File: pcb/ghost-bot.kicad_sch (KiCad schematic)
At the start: 25 parts, among them J1 Conn_01x03_Pin, J2 Conn_01x03_Pin, J3 Conn_01x02_Pin, J4 Conn_01x04_Pin, SW1 SW_Push

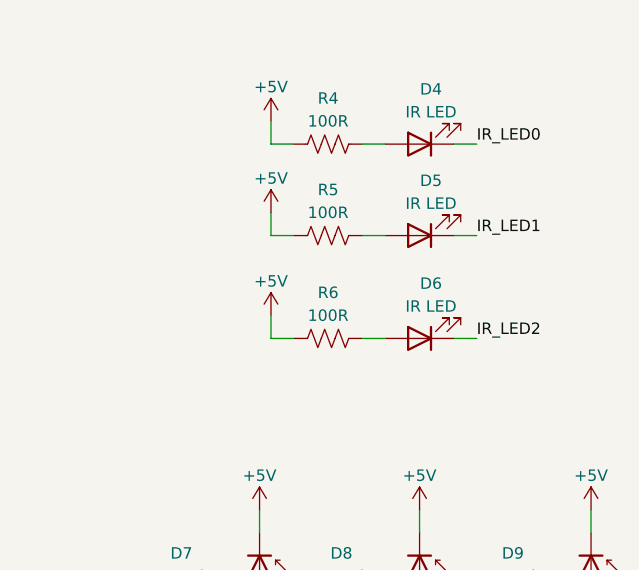
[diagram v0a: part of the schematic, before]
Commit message: Connect IR LEDs to GND
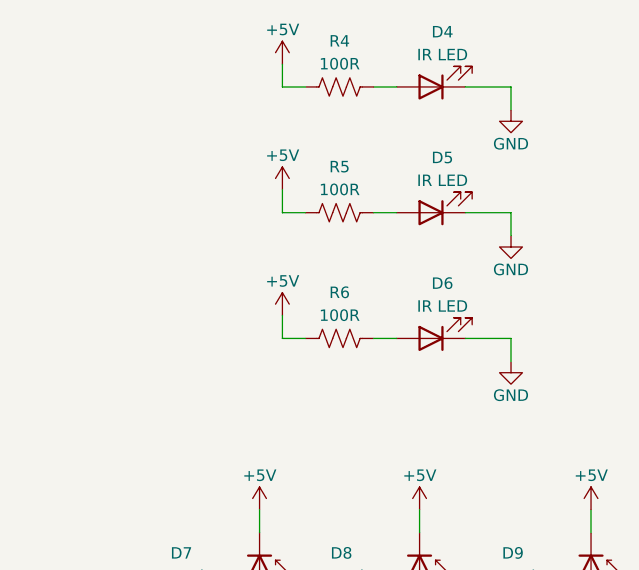
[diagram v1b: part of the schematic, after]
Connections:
- net IR_LED0 is gone; now on net GND: D4.1 (K)
- net IR_LED1 is gone; now on net GND: D5.1 (K)
- net IR_LED2 is gone; now on net GND: D6.1 (K)
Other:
- moved on the sheet: D4, D5, D6, R4, R5, R6

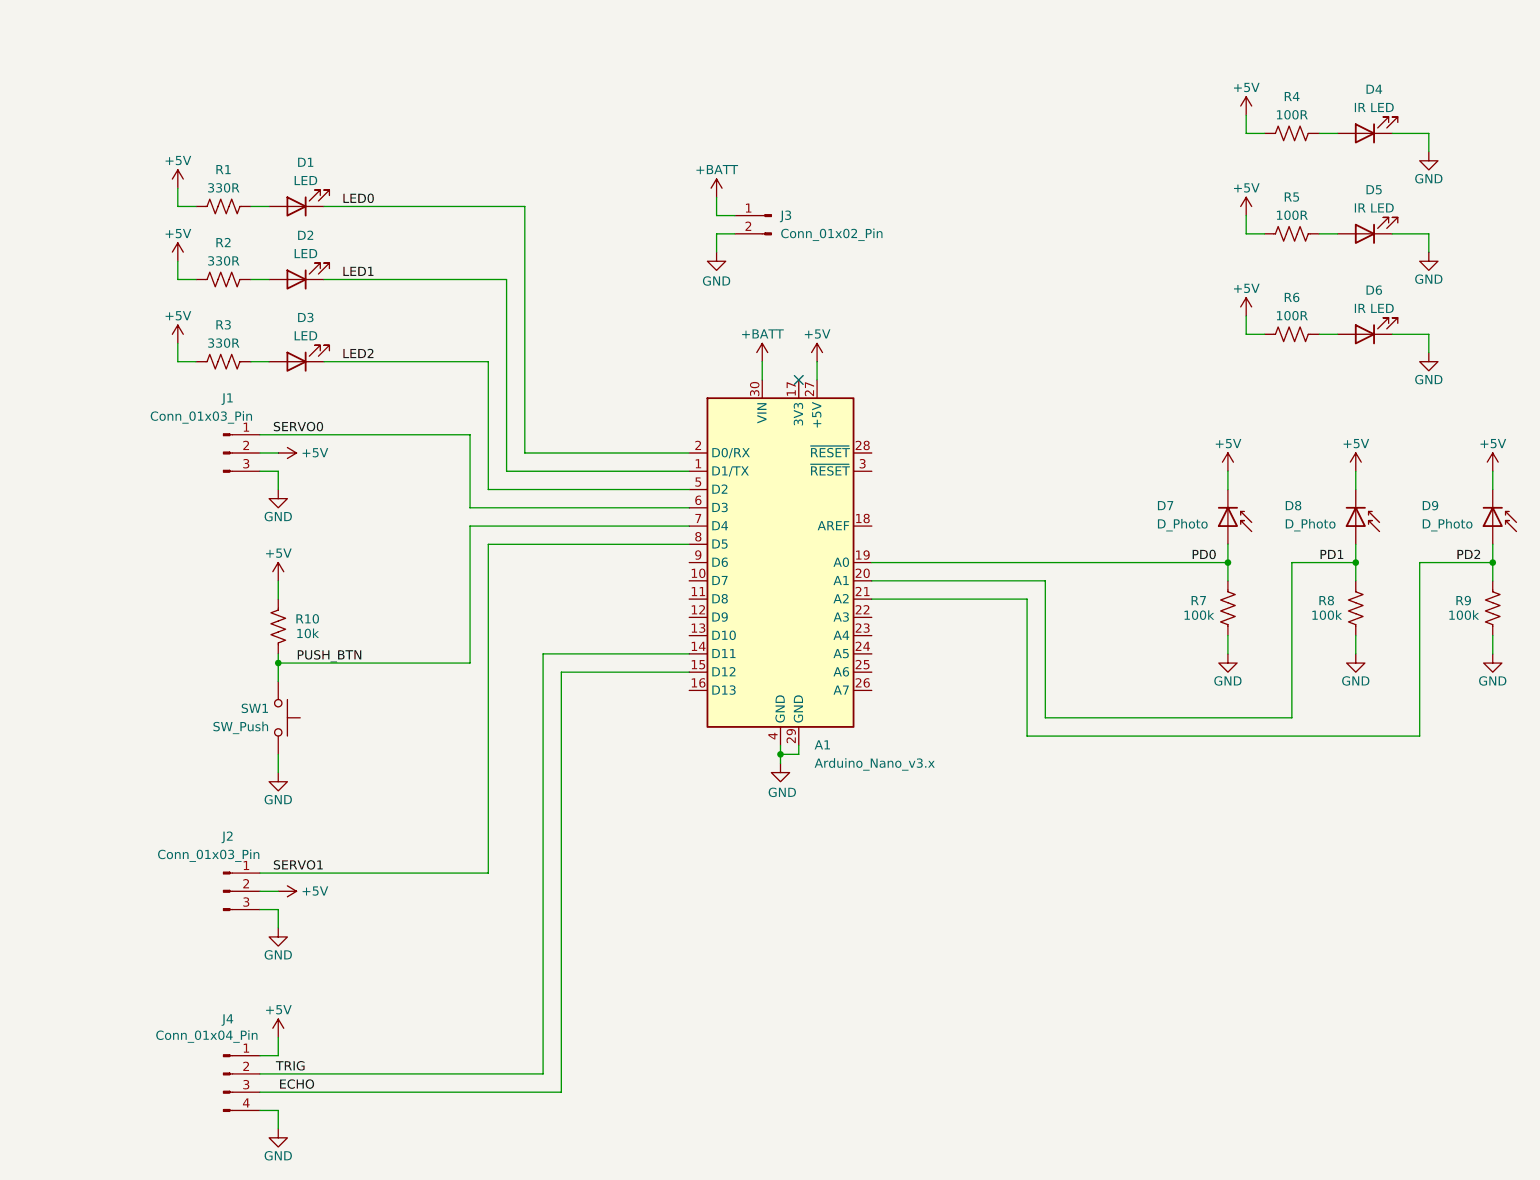
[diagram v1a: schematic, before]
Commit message: Breakout unused pins, add extra power pins
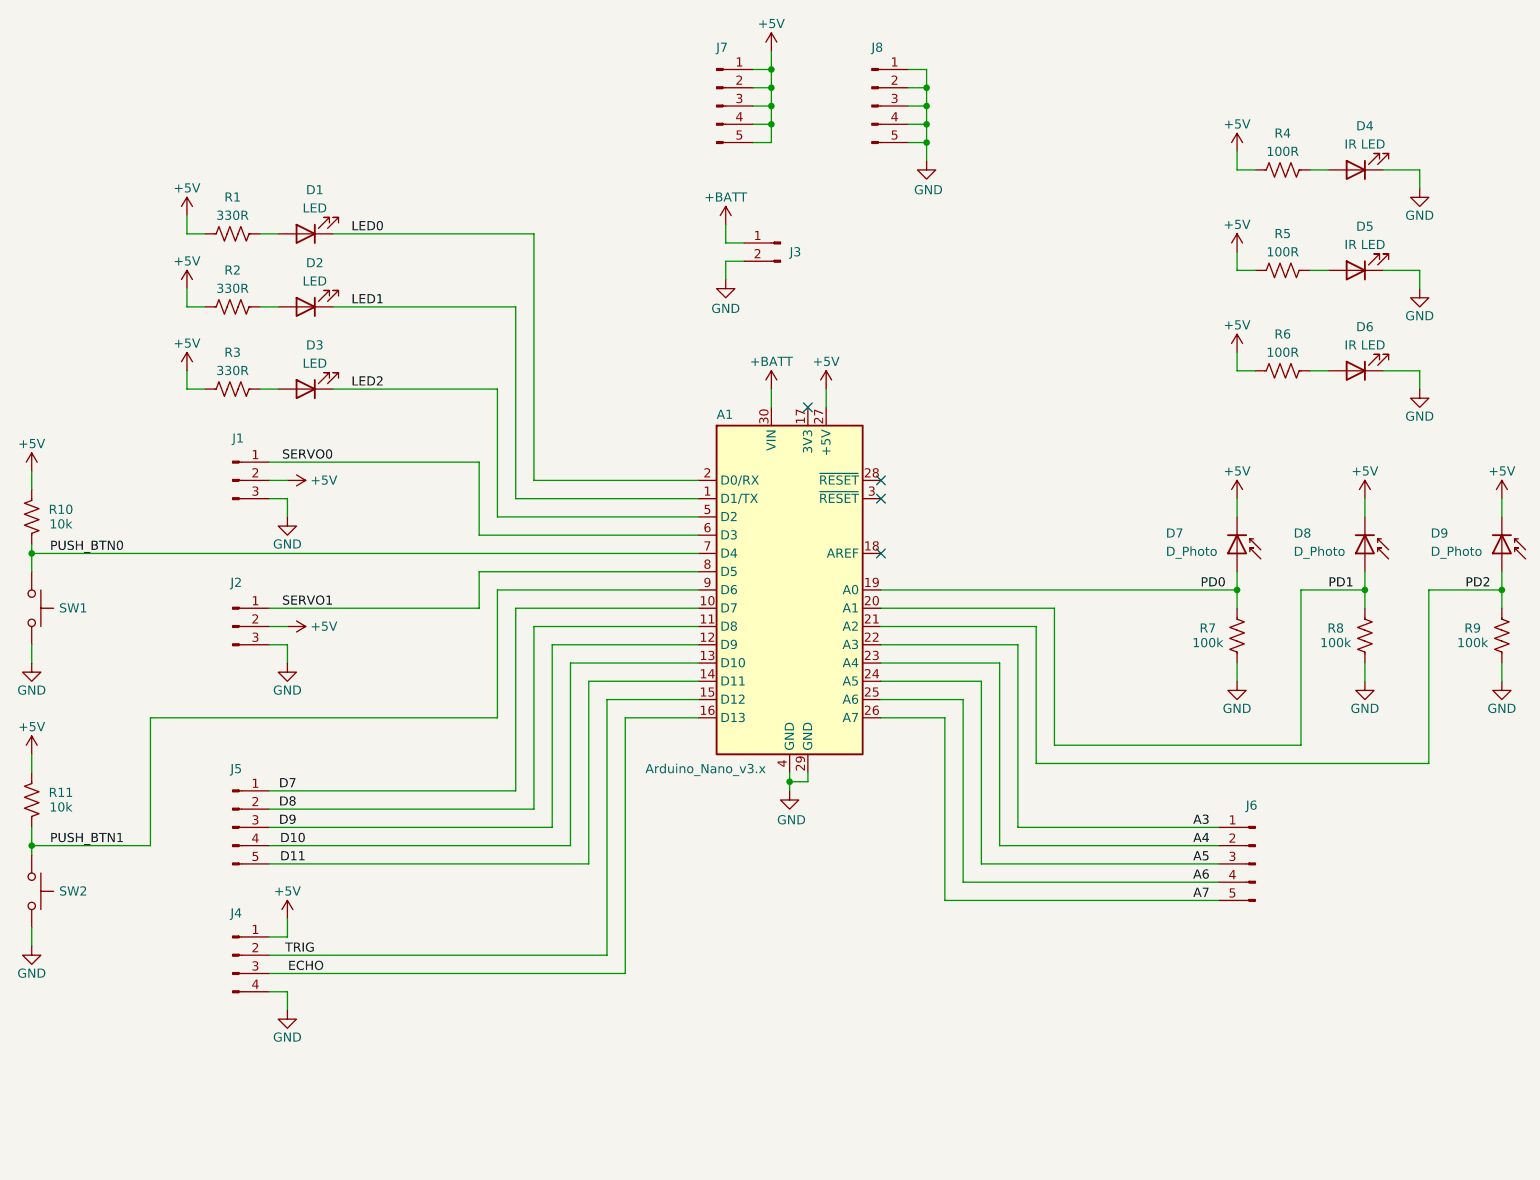
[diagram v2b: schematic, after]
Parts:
- added J5, J6, J7, J8: Conn_01x05_Pin, Connector_PinHeader_2.54mm:PinHeader_1x05_P2.54mm_Vertical, symbol Connector:Conn_01x05_Pin
- added R11: 10k, Resistor_THT:R_Axial_DIN0207_L6.3mm_D2.5mm_P10.16mm_Horizontal, symbol Device:R_US
- added SW2: SW_Push, Button_Switch_THT:SW_PUSH_6mm, symbol Switch:SW_Push
- J1, J2: footprint (none) -> Connector_PinHeader_2.54mm:PinHeader_1x03_P2.54mm_Vertical
- J3: footprint (none) -> Connector_PinHeader_2.54mm:PinHeader_1x02_P2.54mm_Vertical
- J4: footprint (none) -> Connector_PinHeader_2.54mm:PinHeader_1x04_P2.54mm_Vertical
- SW1: footprint (none) -> Button_Switch_THT:SW_PUSH_6mm
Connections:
- net +5V: now also J7.1 (Pin_1), J7.2 (Pin_2), J7.3 (Pin_3), J7.4 (Pin_4), J7.5 (Pin_5), R11.2
- net ECHO: now also A1.16 (D13); no longer A1.15 (D12)
- net GND: now also J8.1 (Pin_1), J8.2 (Pin_2), J8.3 (Pin_3), J8.4 (Pin_4), J8.5 (Pin_5), SW2.1
- net TRIG: now also A1.15 (D12); no longer A1.14 (D11)
- net D7: now reaches A1.10 (D7)
- net D7: now also J5.1 (Pin_1)
- net D8: now reaches A1.11 (D8)
- net D8: now also J5.2 (Pin_2)
- net D9: now reaches A1.12 (D9)
- net D9: now also J5.3 (Pin_3)
- net D10: now reaches A1.13 (D10)
- net D10: now also J5.4 (Pin_4)
- net A3: now reaches A1.22 (A3)
- net A3: now also J6.1 (Pin_1)
- net A4: now reaches A1.23 (A4)
- net A4: now also J6.2 (Pin_2)
- net A5: now reaches A1.24 (A5)
- net A5: now also J6.3 (Pin_3)
- net A6: now reaches A1.25 (A6)
- net A6: now also J6.4 (Pin_4)
- net A7: now reaches A1.26 (A7)
- net A7: now also J6.5 (Pin_5)
- net PUSH_BTN1: now reaches A1.9 (D6)
- net PUSH_BTN1: now also R11.1, SW2.2
- net PUSH_BTN renamed PUSH_BTN0
- new net D11: A1.14 (D11), J5.5 (Pin_5)
- no-connect marks 1 -> 4
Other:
- title: (none) -> Ghost Bot
- moved on the sheet: A1, D1, D2, D3, D4, D5, D6, D7, D8, D9, J1, J2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

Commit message: Simplify circuit, add battery holder mounting points
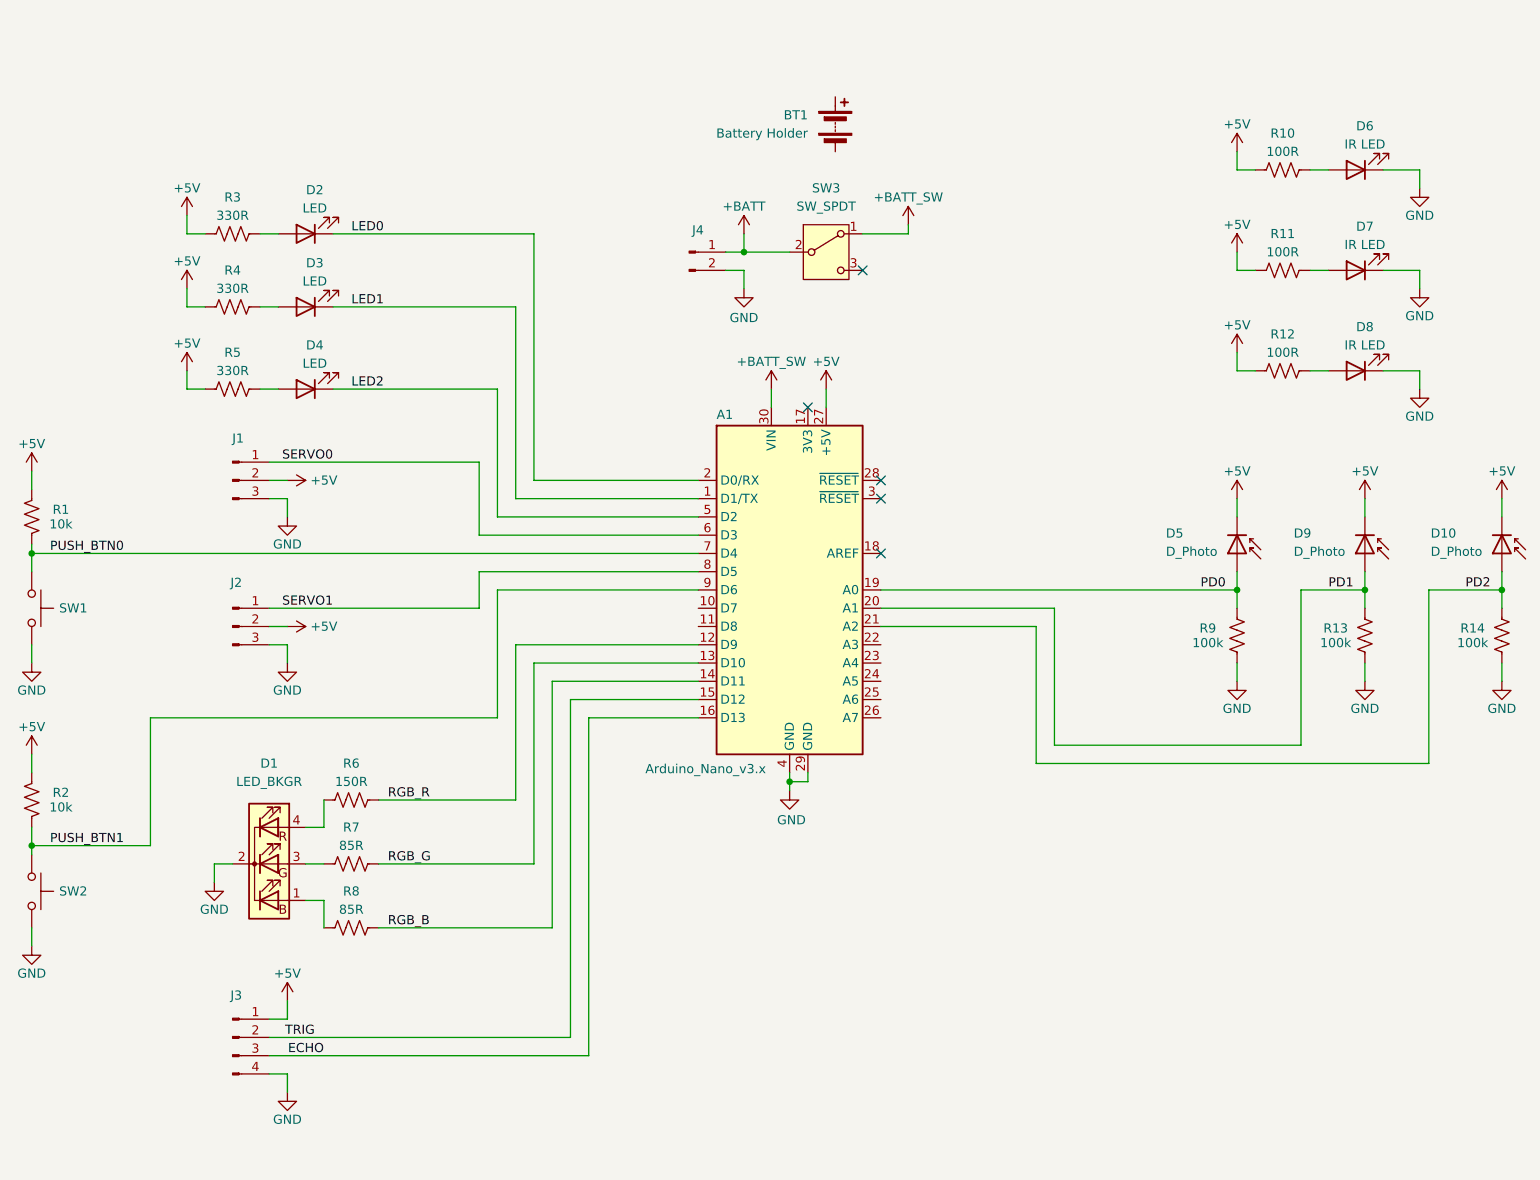
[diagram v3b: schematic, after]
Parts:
- removed J5, J6, J7, J8: Conn_01x05_Pin, Connector_PinHeader_2.54mm:PinHeader_1x05_P2.54mm_Vertical, symbol Connector:Conn_01x05_Pin
- added BT1: Battery Holder, ghost-bot-footprints:Keystone 2478 Battery Holder, symbol ghost-bot-symbols:Battery Holder
- added D1: LED_BKGR, LED_THT:LED_D5.0mm-4_RGB, symbol Device:LED_BKGR
- added R6: 150R, Resistor_THT:R_Axial_DIN0207_L6.3mm_D2.5mm_P10.16mm_Horizontal, symbol Device:R_US
- added R7, R8: 85R, Resistor_THT:R_Axial_DIN0207_L6.3mm_D2.5mm_P10.16mm_Horizontal, symbol Device:R_US
- added SW3: SW_SPDT, Button_Switch_THT:SW_Slide_SPDT_Straight_CK_OS102011MS2Q, symbol Switch:SW_SPDT
- D10: renamed from D9; footprint LED_THT:LED_D5.0mm -> LED_THT:LED_D5.0mm_Clear
- D5: renamed from D7; footprint LED_THT:LED_D5.0mm -> LED_THT:LED_D5.0mm_Clear
- D6: renamed from D4; footprint LED_THT:LED_D5.0mm -> LED_THT:LED_D5.0mm_IRBlack
- D7: renamed from D5; footprint LED_THT:LED_D5.0mm -> LED_THT:LED_D5.0mm_IRBlack
- D8: renamed from D6; footprint LED_THT:LED_D5.0mm -> LED_THT:LED_D5.0mm_IRBlack
- D9: renamed from D8; footprint LED_THT:LED_D5.0mm -> LED_THT:LED_D5.0mm_Clear
- renumbered D1 to D2, D2 to D3, D3 to D4, J4 to J3, J3 to J4, R10 to R1, R4 to R10, R5 to R11, R6 to R12, R8 to R13, R9 to R14, R11 to R2, R1 to R3, R2 to R4, R3 to R5, R7 to R9
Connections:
- net +BATT: now also SW3.2 (B); no longer A1.30 (VIN)
- net GND: now also D1.2 (K)
- net A3: no longer names the net of A1.22 (A3)
- net A4: no longer names the net of A1.23 (A4)
- net A5: no longer names the net of A1.24 (A5)
- net A6: no longer names the net of A1.25 (A6)
- net A7: no longer names the net of A1.26 (A7)
- net D10 renamed RGB_G
- net RGB_G: now also R7.2
- net D11 renamed RGB_B
- net RGB_B: now also R8.2
- net D7: no longer names the net of A1.10 (D7)
- net D8: no longer names the net of A1.11 (D8)
- net D9 renamed RGB_R
- net RGB_R: now also R6.2
- new net: D1.1 (BA), R8.1
- new net: D1.4 (RA), R6.1
- new net: D1.3 (GA), R7.1
- new net +BATT_SW: A1.30 (VIN), SW3.1 (A)
- no-connect marks 4 -> 5
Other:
- moved on the sheet: J3, J4
